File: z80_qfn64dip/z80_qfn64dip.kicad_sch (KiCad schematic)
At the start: 28 parts, among them U1 Caravel_QFN, U2 Z80CPU, U3 AZ1117-3.3, U4 AP2112K-1.8, X1 10MHz

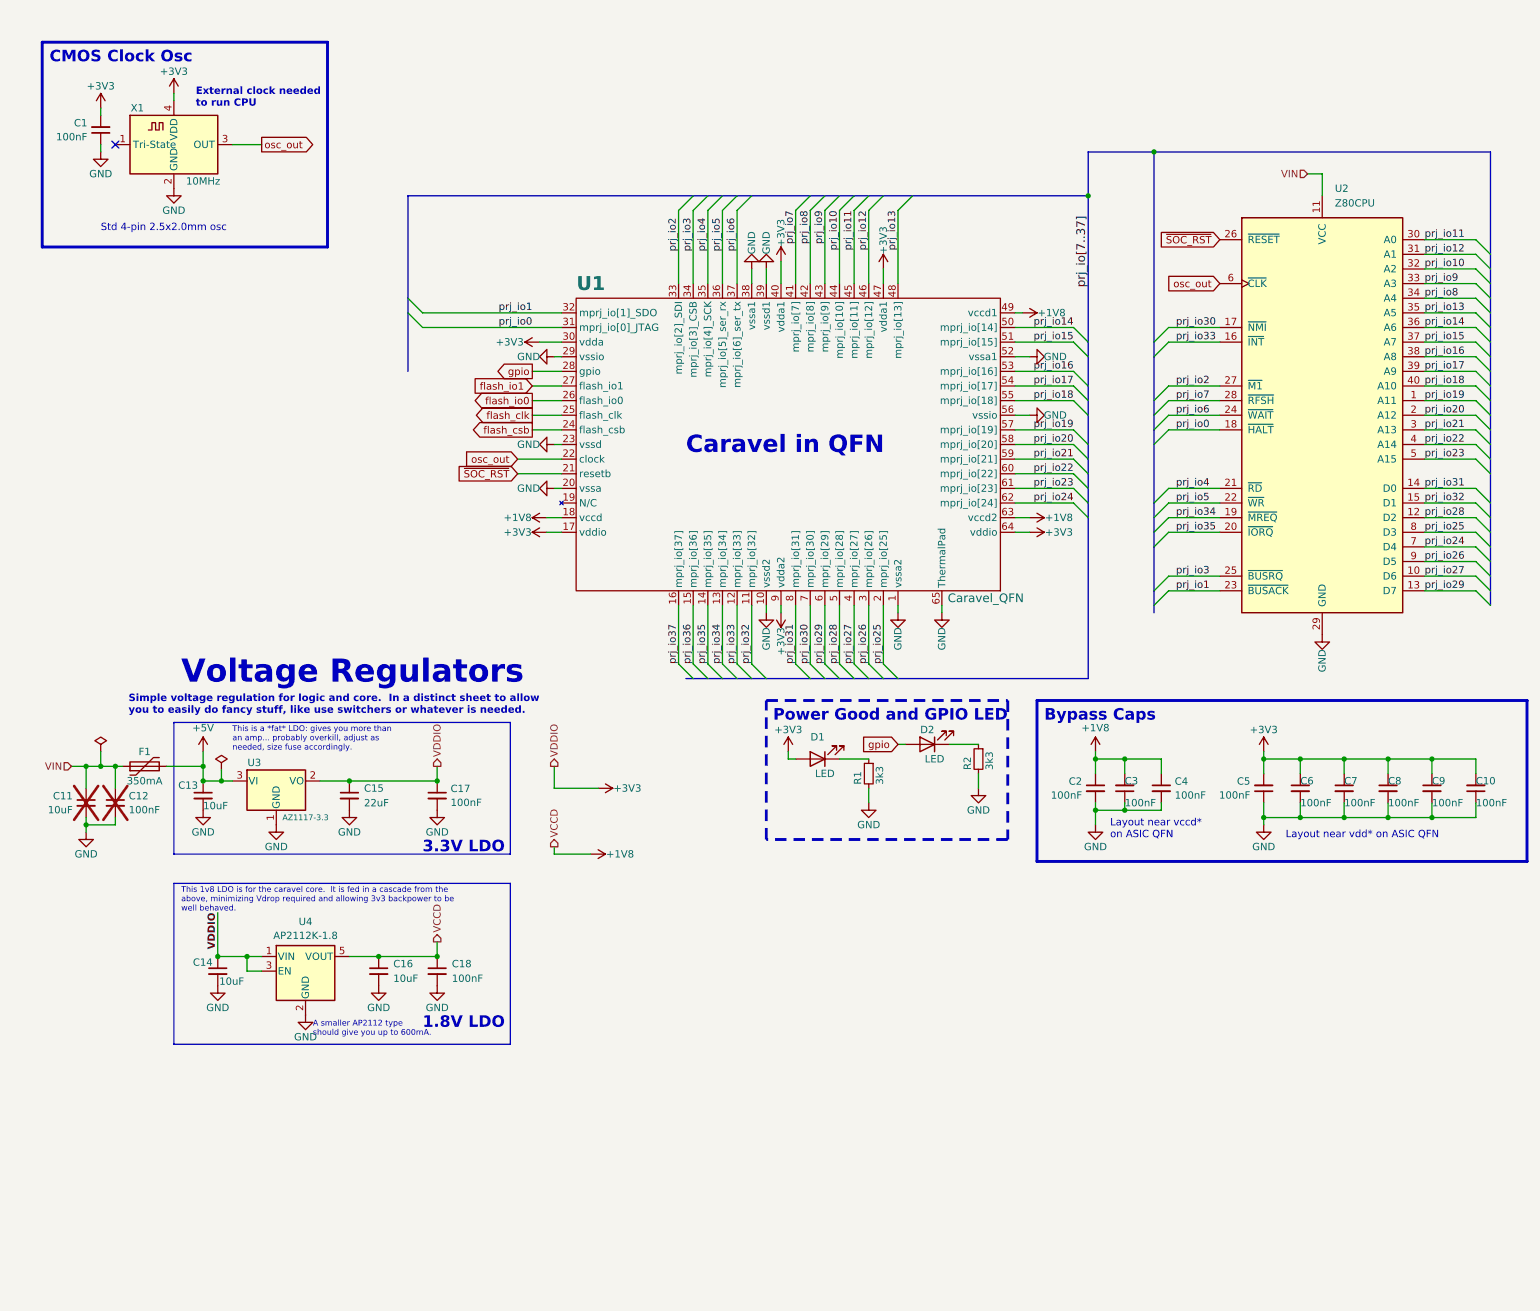
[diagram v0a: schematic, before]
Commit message: add flash and move to 4 layers
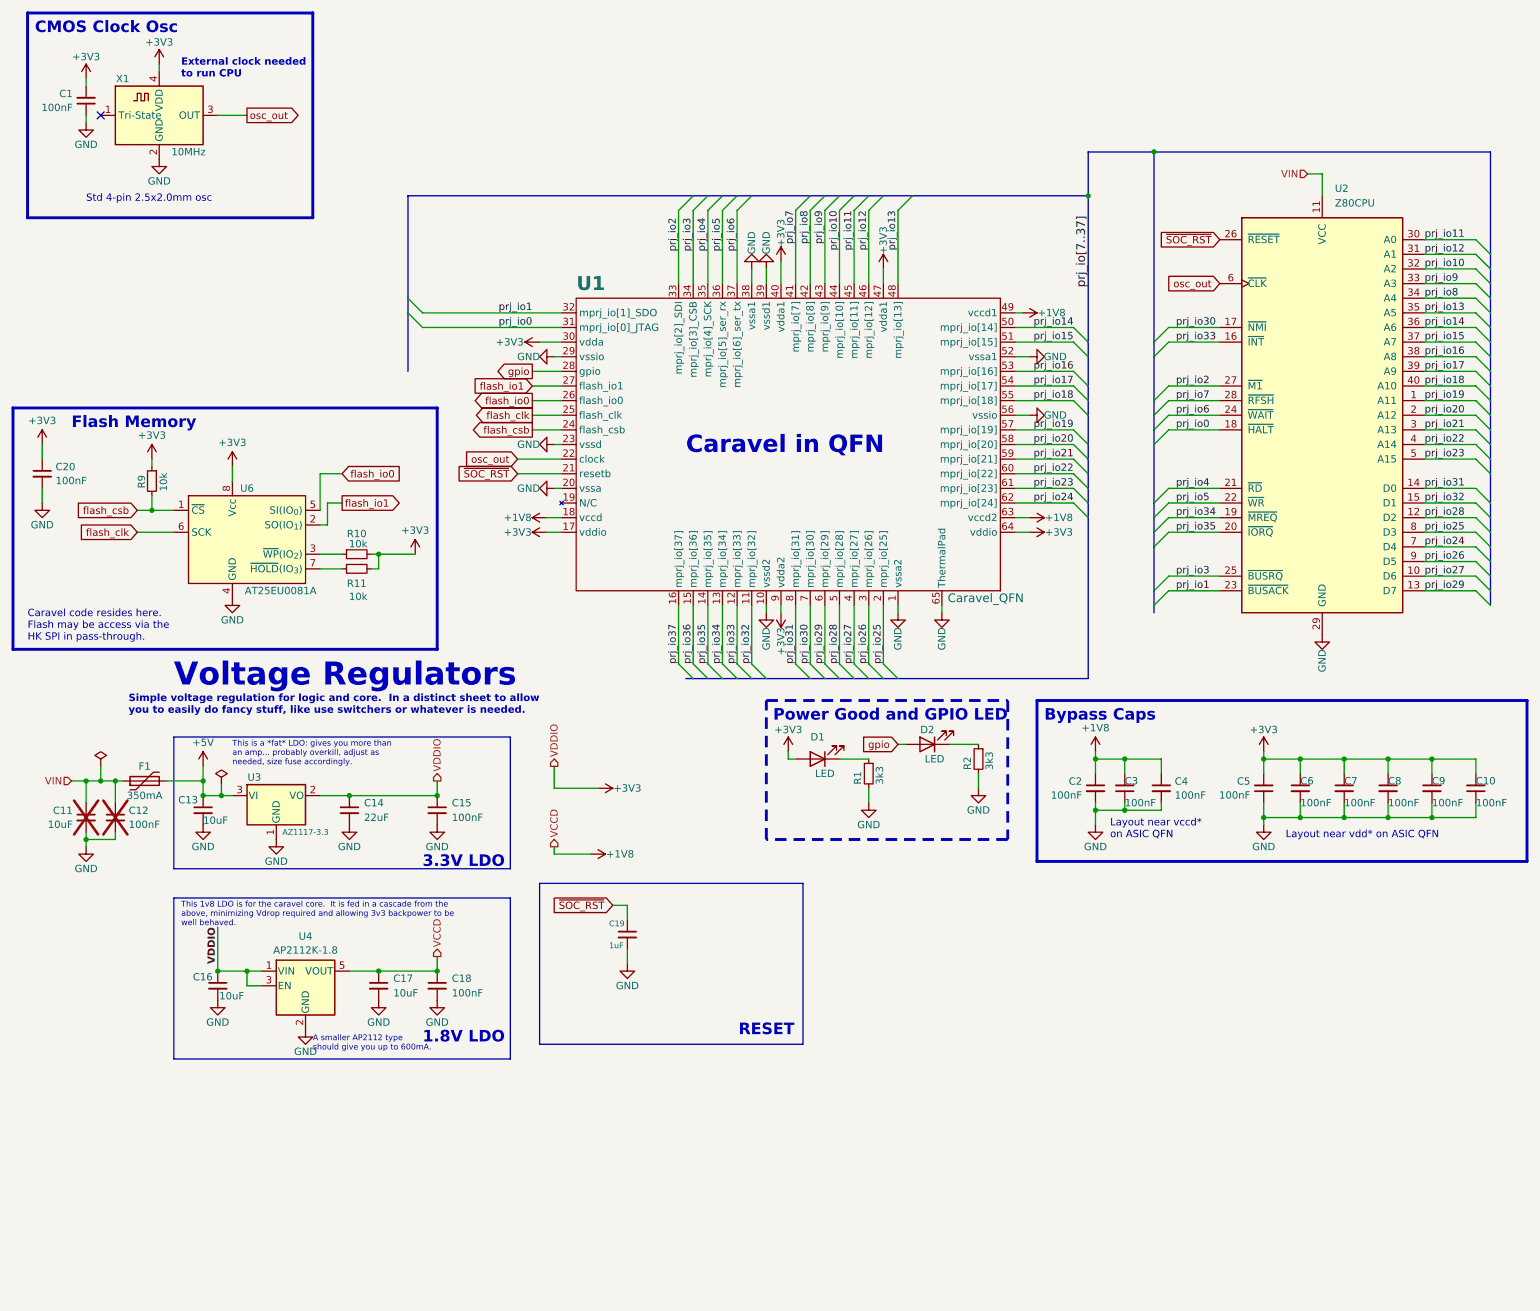
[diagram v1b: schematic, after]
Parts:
- added C19: 1uF, Capacitor_SMD:C_0603_1608Metric, symbol Device:C_Small
- added C20: 100nF, Capacitor_SMD:C_0603_1608Metric, symbol Device:C_Small
- added R10: 10k, Resistor_SMD:R_0603_1608Metric, symbol Device:R_Small
- added R11, R9: 10k, Resistor_SMD:R_0402_1005Metric, symbol Device:R_Small
- added U6: AT25EU0081A, KiCadModels:UDFN-8-1EP-2x3mm_P0.5mm_EP1.6x0.2mm, symbol caravel:AT25EU0081A
- renumbered C15 to C14, C17 to C15, C14 to C16, C16 to C17
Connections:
- net +3V3: now also C20.1, R10.2, R11.2, R9.1, U6.8 (Vcc)
- net GND: now also C19.2, C20.2, U6.4 (GND)
- net flash_clk: now also U6.6 (SCK)
- net flash_csb: now also R9.2, U6.1 (~{CS})
- net flash_io0: now also U6.5 (SI(IO_{0}))
- net flash_io1: now also U6.2 (SO(IO_{1}))
- net ~{SOC_RST}: now also C19.1
- new net: R11.1, U6.7 (~{HOLD}(IO_{3}))
- new net: R10.1, U6.3 (~{WP}(IO_{2}))
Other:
- note added: "Caravel code resides here. Flash may be access via the HK SPI in pass-through."
- note added: "Flash Memory"
- note added: "RESET"
- moved on the sheet: C1, C11, C12, C13, C14, C15, C16, C17, C18, F1, U3, U4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

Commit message: hand solder pads for bottom caps, minor tweaks to layout
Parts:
- C10, C2, C20, C5, C6, C7, C8, C9: footprint Capacitor_SMD:C_0603_1608Metric -> Capacitor_SMD:C_0603_1608Metric_Pad1.08x0.95mm_HandSolder
- R10: footprint Resistor_SMD:R_0603_1608Metric -> Resistor_SMD:R_0402_1005Metric
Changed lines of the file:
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@@
 			)
 		)
-		(property "Footprint" "Capacitor_SMD:C_0603_1608Metric"
+		(property "Footprint" "Capacitor_SMD:C_0603_1608Metric_Pad1.08x0.95mm_HandSolder"
 			(at 251.46 148.59 0)
 			(effects
@@
 			)
 		)
-		(property "Footprint" "Capacitor_SMD:C_0603_1608Metric"
+		(property "Footprint" "Capacitor_SMD:C_0603_1608Metric_Pad1.08x0.95mm_HandSolder"
 			(at 236.22 148.59 0)
 			(effects
@@
 			)
 		)
-		(property "Footprint" "Capacitor_SMD:C_0603_1608Metric"
+		(property "Footprint" "Capacitor_SMD:C_0603_1608Metric_Pad1.08x0.95mm_HandSolder"
 			(at 17.78 93.98 0)
 			(effects
@@
 			)
 		)
-		(property "Footprint" "Capacitor_SMD:C_0603_1608Metric"
+		(property "Footprint" "Capacitor_SMD:C_0603_1608Metric_Pad1.08x0.95mm_HandSolder"
 			(at 200.66 148.59 0)
 			(effects
@@
 			)
 		)
-		(property "Footprint" "Capacitor_SMD:C_0603_1608Metric"
+		(property "Footprint" "Capacitor_SMD:C_0603_1608Metric_Pad1.08x0.95mm_HandSolder"
 			(at 259.08 148.59 0)
 			(effects
@@
 			)
 		)
-		(property "Footprint" "Capacitor_SMD:C_0603_1608Metric"
+		(property "Footprint" "Capacitor_SMD:C_0603_1608Metric_Pad1.08x0.95mm_HandSolder"
 			(at 229.87 148.59 0)
 			(effects
@@
 			)
 		)
-		(property "Footprint" "Capacitor_SMD:C_0603_1608Metric"
+		(property "Footprint" "Capacitor_SMD:C_0603_1608Metric_Pad1.08x0.95mm_HandSolder"
 			(at 266.7 148.59 0)
 			(effects
@@
 			)
 		)
-		(property "Footprint" "Capacitor_SMD:C_0603_1608Metric"
+		(property "Footprint" "Capacitor_SMD:C_0603_1608Metric_Pad1.08x0.95mm_HandSolder"
 			(at 243.84 148.59 0)
 			(effects
@@
 			)
 		)
-		(property "Footprint" "Resistor_SMD:R_0603_1608Metric"
+		(property "Footprint" "Resistor_SMD:R_0402_1005Metric"
 			(at 72.39 107.95 0)
 			(effects

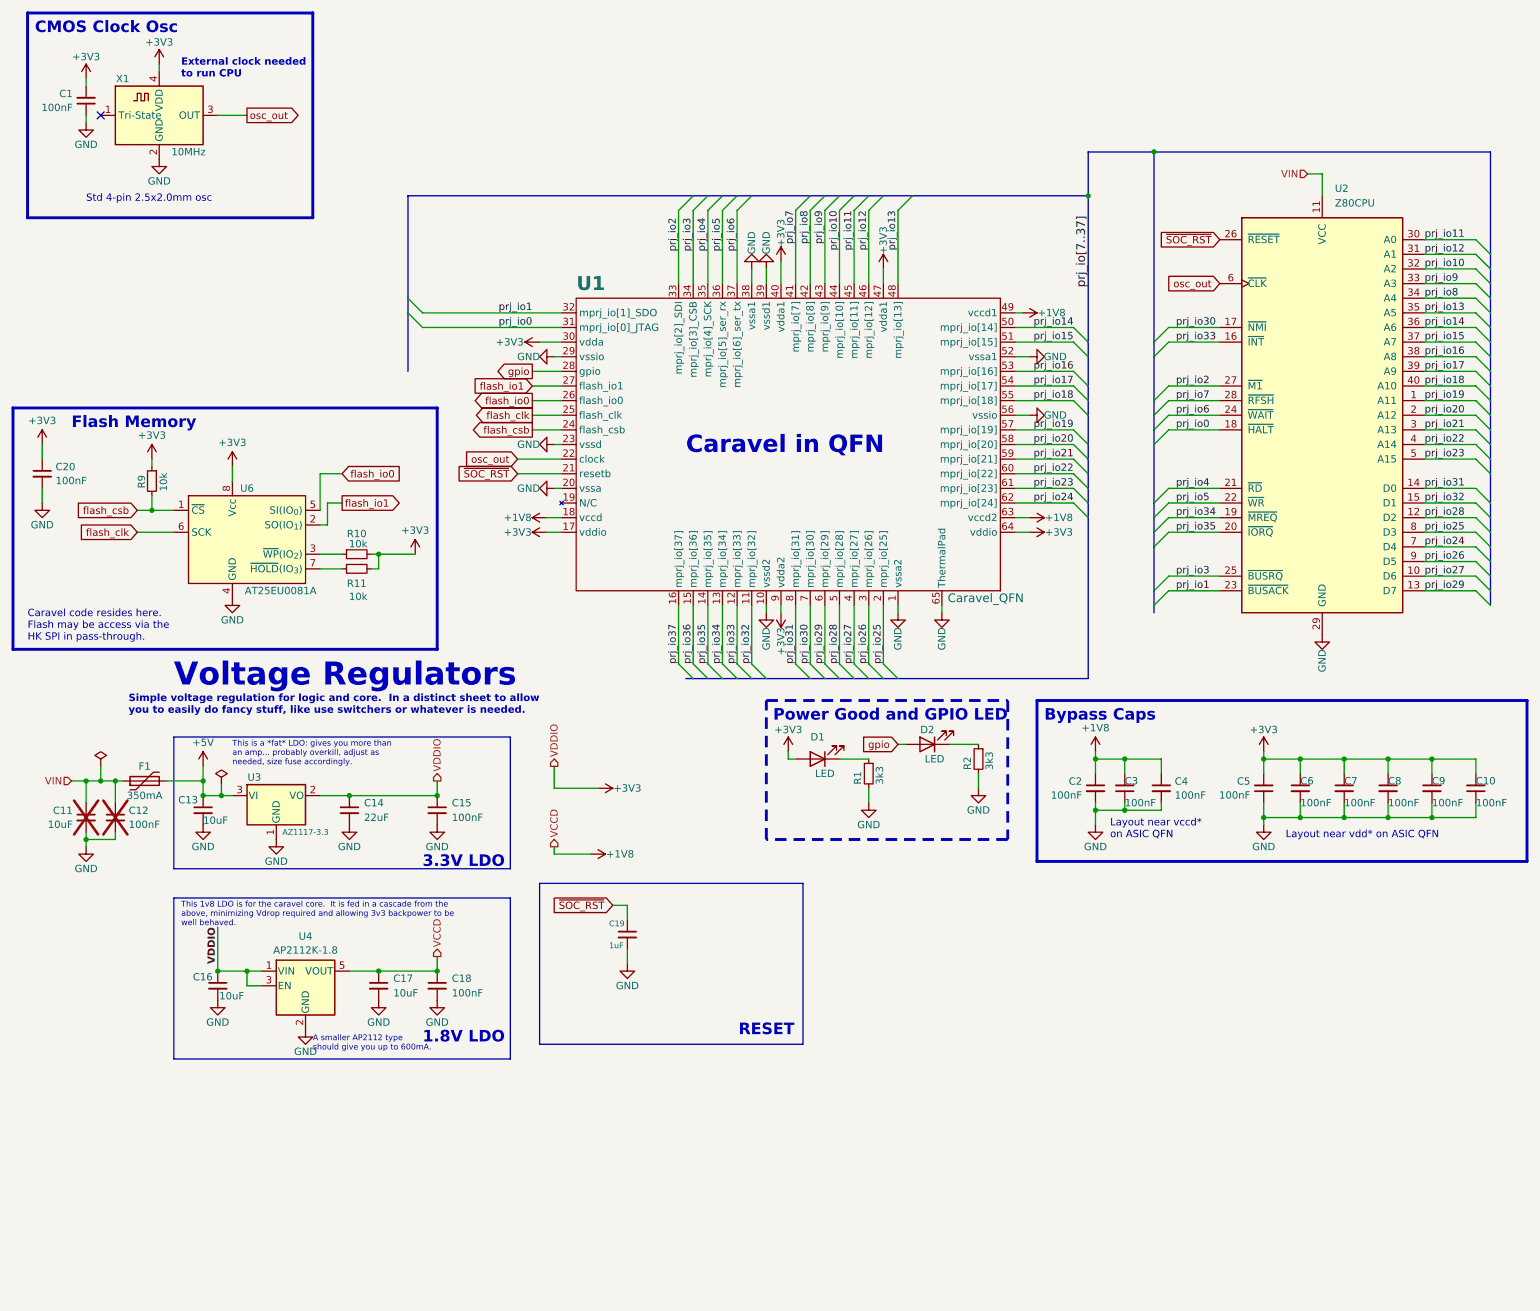
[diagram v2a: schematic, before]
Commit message: jtag/spi connector
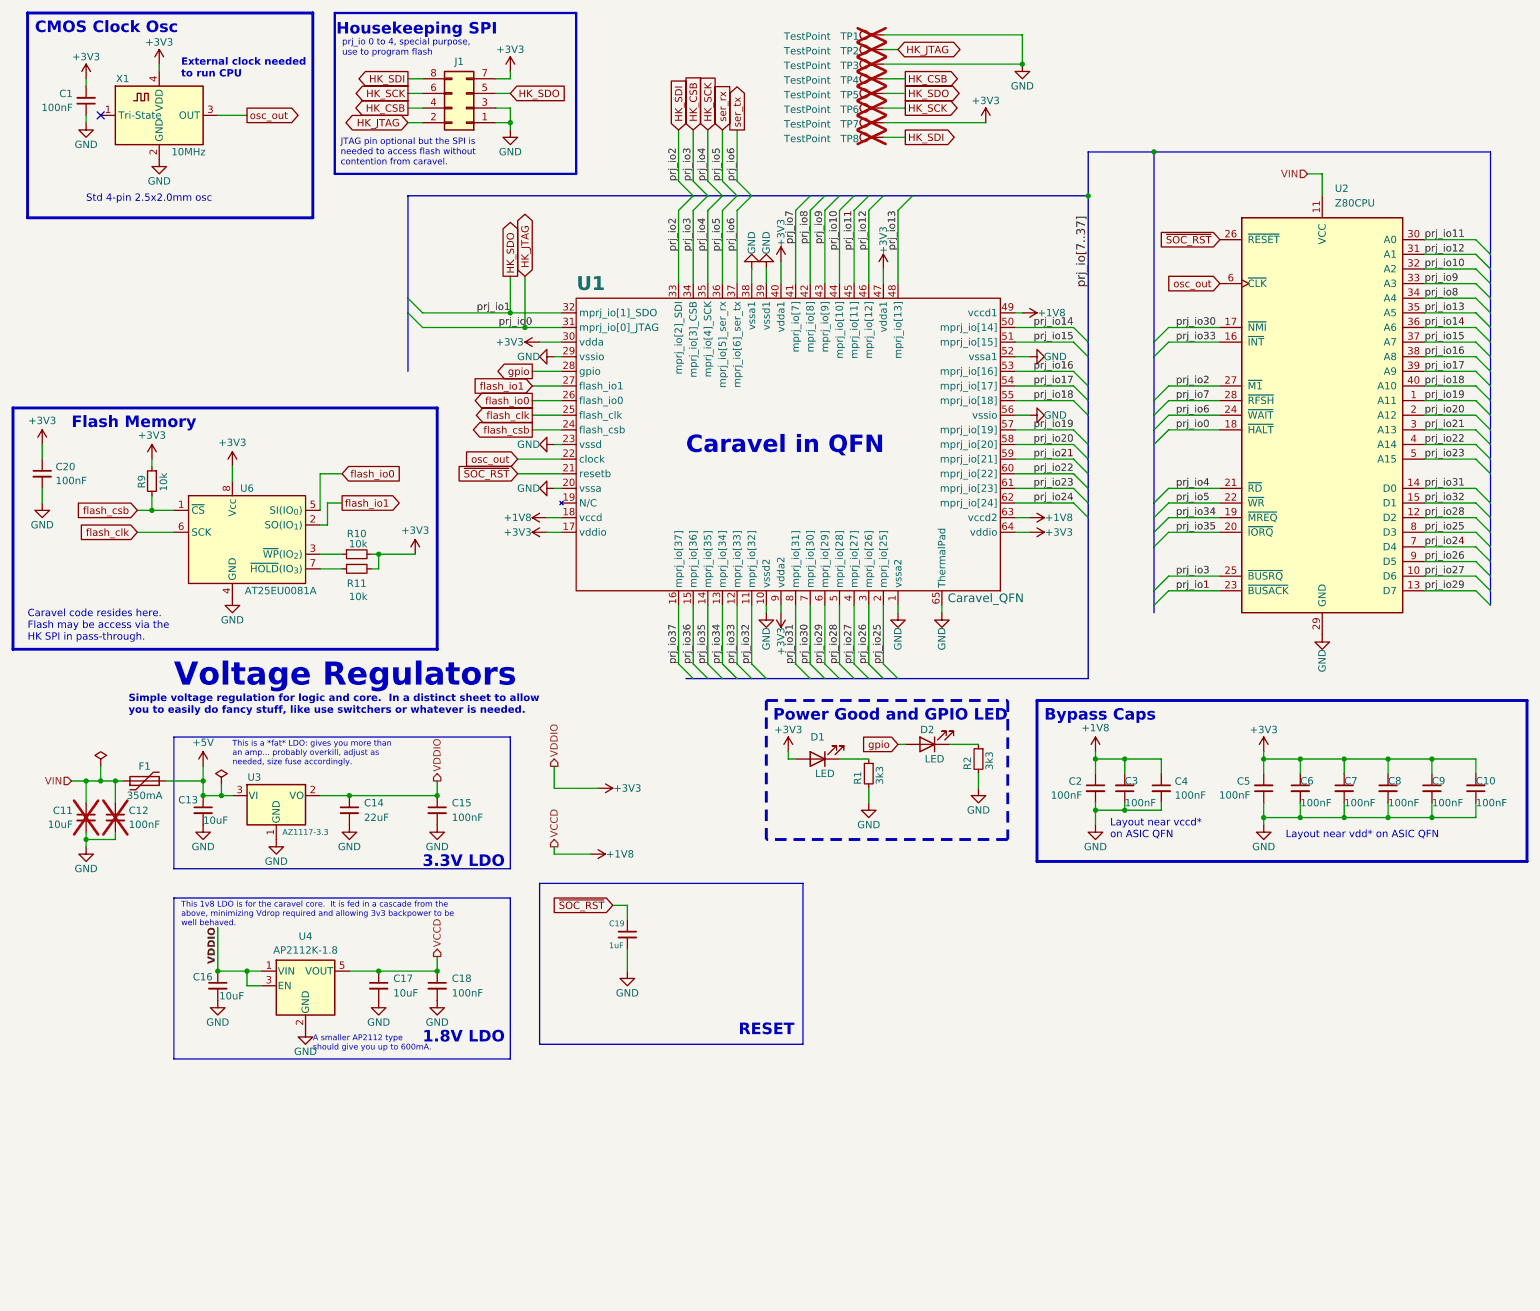
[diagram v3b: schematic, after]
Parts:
- added J1: Conn_02x04_Odd_Even, Connector_PinHeader_1.27mm:PinHeader_2x04_P1.27mm_Vertical, symbol Connector_Generic:Conn_02x04_Odd_Even
- added TP1, TP2, TP3, TP4, TP5, TP6, TP7, TP8: TestPoint, TestPoint:TestPoint_Pad_D1.0mm, symbol Connector:TestPoint
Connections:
- net +3V3: now also J1.7 (Pin_7), TP7.1
- net GND: now also J1.1 (Pin_1), J1.3 (Pin_3), TP1.1, TP3.1
- net prj_io0 renamed HK_JTAG
- net HK_JTAG: now also J1.2 (Pin_2), TP2.1
- net prj_io1 renamed HK_SDO
- net HK_SDO: now also J1.5 (Pin_5), TP5.1
- net prj_io2 renamed HK_SDI
- net HK_SDI: now also J1.8 (Pin_8), TP8.1
- net prj_io3 renamed HK_CSB
- net HK_CSB: now also J1.4 (Pin_4), TP4.1
- net prj_io4 renamed HK_SCK
- net HK_SCK: now also J1.6 (Pin_6), TP6.1
- net prj_io5 renamed ser_rx
- net prj_io6 renamed ser_tx
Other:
- note added: "Housekeeping SPI"
- note added: "JTAG pin optional but the SPI is needed to access flash without contention from caravel."
- note added: "prj_io 0 to 4, special purpose, use to program flash"

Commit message: remove crystal; testpoints connected directly to flash
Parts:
- added TP10: io0, TestPoint:TestPoint_Pad_D1.0mm, symbol Connector:TestPoint
- added TP11: clk, TestPoint:TestPoint_Pad_D1.0mm, symbol Connector:TestPoint
- added TP12: csb, TestPoint:TestPoint_Pad_D1.0mm, symbol Connector:TestPoint
- added TP13: GND, TestPoint:TestPoint_Pad_D1.0mm, symbol Connector:TestPoint
- added TP9: io1, TestPoint:TestPoint_Pad_D1.0mm, symbol Connector:TestPoint
- C1, X1: now not fitted
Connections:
- net GND: now also TP13.1
- net HK_CSB: no longer U2.25 (~{BUSRQ})
- net HK_JTAG: now also U2.26 (~{RESET}); no longer U2.18 (~{HALT})
- net flash_clk: now also TP11.1
- net flash_csb: now also TP12.1
- net flash_io0: now also TP10.1
- net flash_io1: now also TP9.1
- net prj_io36: now also U2.18 (~{HALT})
- net prj_io37: now also U2.25 (~{BUSRQ})
- net ~{SOC_RST}: no longer U2.26 (~{RESET})

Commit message: tweak connections due to changed caravel pinout
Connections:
- net prj_io30: now also U2.15 (D1); no longer U2.17 (~{NMI})
- net prj_io32: now also U2.17 (~{NMI}); no longer U2.15 (D1)
- net prj_io34: now also U2.18 (~{HALT}); no longer U2.19 (~{MREQ})
- net prj_io35: now also U2.19 (~{MREQ}); no longer U2.20 (~{IORQ})
- net prj_io36: now also U2.20 (~{IORQ}); no longer U2.18 (~{HALT})
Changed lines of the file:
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@@
 		)
 	)
-	(label "prj_io36"
+	(label "prj_io34"
 		(at 214.63 86.36 0)
 		(fields_autoplaced yes)
@@
 		)
 	)
-	(label "prj_io30"
+	(label "prj_io32"
 		(at 214.63 68.58 0)
 		(fields_autoplaced yes)
@@
 		)
 	)
-	(label "prj_io35"
+	(label "prj_io36"
 		(at 214.63 104.14 0)
 		(fields_autoplaced yes)
@@
 		)
 	)
-	(label "prj_io32"
+	(label "prj_io30"
 		(at 257.81 99.06 0)
 		(fields_autoplaced yes)
@@
 		)
 	)
-	(label "prj_io34"
+	(label "prj_io35"
 		(at 214.63 101.6 0)
 		(fields_autoplaced yes)
